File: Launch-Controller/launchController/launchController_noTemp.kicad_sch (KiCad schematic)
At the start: 124 parts, among them J1 Conn_01x05_Pin, J10 Conn_01x05_Pin, J11 Raspberry_Pi_5, J13 26 pin Dsub, J14 DB25_Plug, J15 Conn_01x03_Pin, J16 DB25_Plug, J17 DB25_Plug, J18 Conn_01x03_Pin, J2 Conn_01x05_Pin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

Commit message: polished launch controller layout
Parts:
- J1, J10, J2, J3, J4, J5, J6, J7, J8, J9: footprint launch_controller:Relay Connector -> launch_controller:RelaySwitch Connector
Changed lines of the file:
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@@
 			)
 		)
-		(property "Footprint" "launch_controller:Relay Connector"
+		(property "Footprint" "launch_controller:RelaySwitch Connector"
 			(at 25.4 204.47 0)
 			(effects
@@
 			)
 		)
-		(property "Footprint" "launch_controller:Relay Connector"
+		(property "Footprint" "launch_controller:RelaySwitch Connector"
 			(at 25.4 166.37 0)
 			(effects
@@
 			)
 		)
-		(property "Footprint" "launch_controller:Relay Connector"
+		(property "Footprint" "launch_controller:RelaySwitch Connector"
 			(at 25.4 147.32 0)
 			(effects
@@
 			)
 		)
-		(property "Footprint" "launch_controller:Relay Connector"
+		(property "Footprint" "launch_controller:RelaySwitch Connector"
 			(at 25.4 53.34 0)
 			(effects
@@
 			)
 		)
-		(property "Footprint" "launch_controller:Relay Connector"
+		(property "Footprint" "launch_controller:RelaySwitch Connector"
 			(at 25.4 72.39 0)
 			(effects
@@
 			)
 		)
-		(property "Footprint" "launch_controller:Relay Connector"
+		(property "Footprint" "launch_controller:RelaySwitch Connector"
 			(at 25.4 34.29 0)
 			(effects
@@
 			)
 		)
-		(property "Footprint" "launch_controller:Relay Connector"
+		(property "Footprint" "launch_controller:RelaySwitch Connector"
 			(at 25.4 185.42 0)
 			(effects
@@
 			)
 		)
-		(property "Footprint" "launch_controller:Relay Connector"
+		(property "Footprint" "launch_controller:RelaySwitch Connector"
 			(at 25.4 91.44 0)
 			(effects
@@
 			)
 		)
-		(property "Footprint" "launch_controller:Relay Connector"
+		(property "Footprint" "launch_controller:RelaySwitch Connector"
 			(at 25.4 109.22 0)
 			(effects
@@
 			)
 		)
-		(property "Footprint" "launch_controller:Relay Connector"
+		(property "Footprint" "launch_controller:RelaySwitch Connector"
 			(at 25.4 128.27 0)
 			(effects

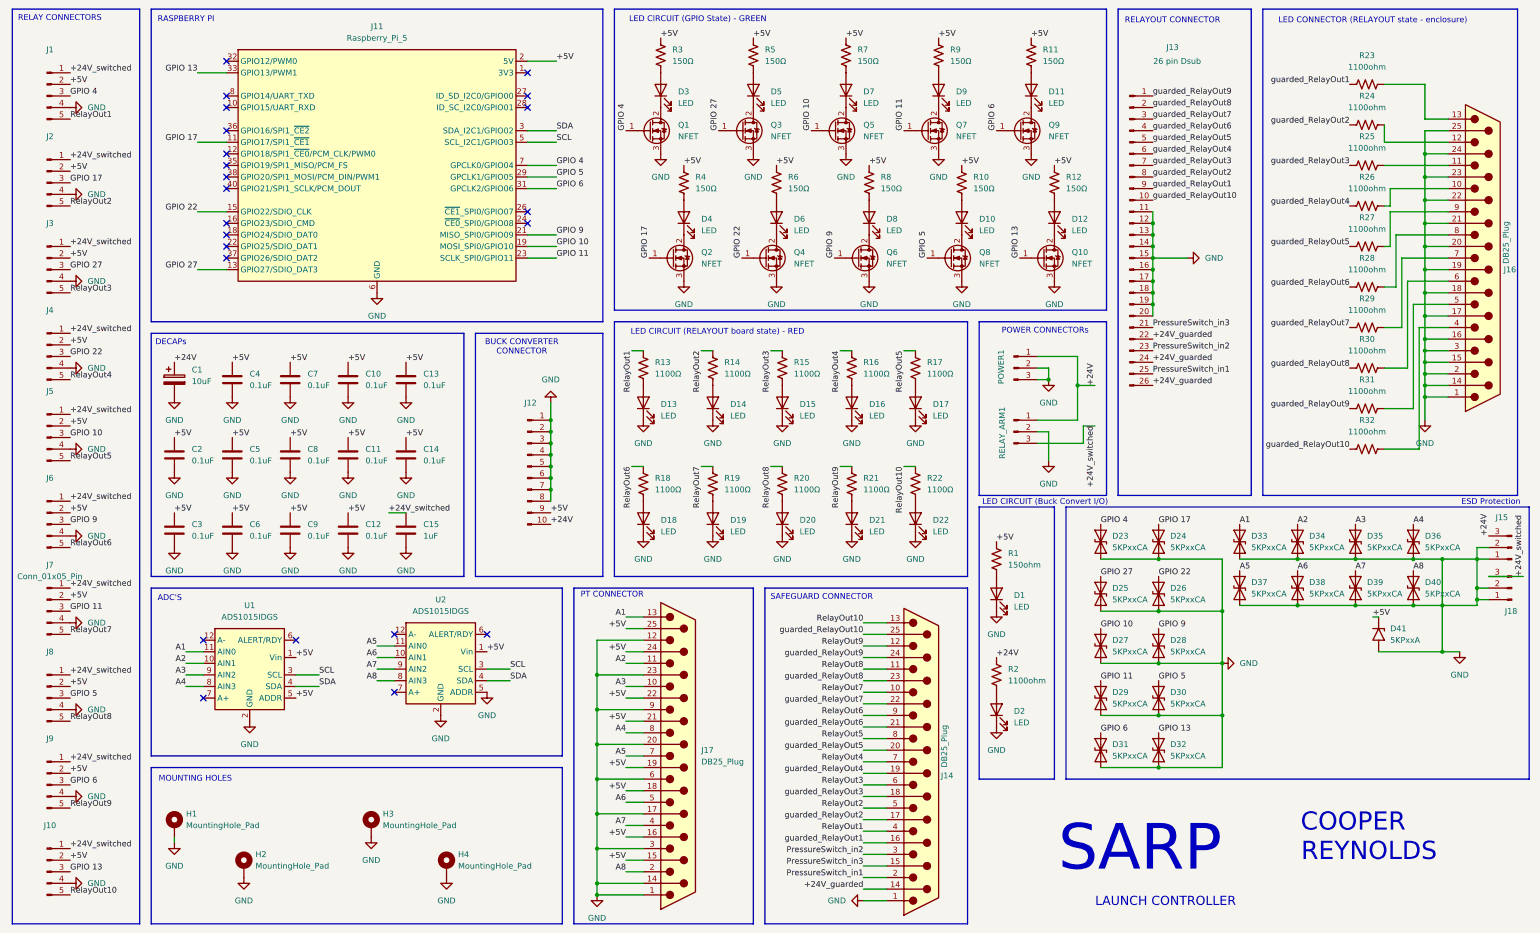
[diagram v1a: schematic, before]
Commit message: logic shifter in LC, cleaning up buck_5v
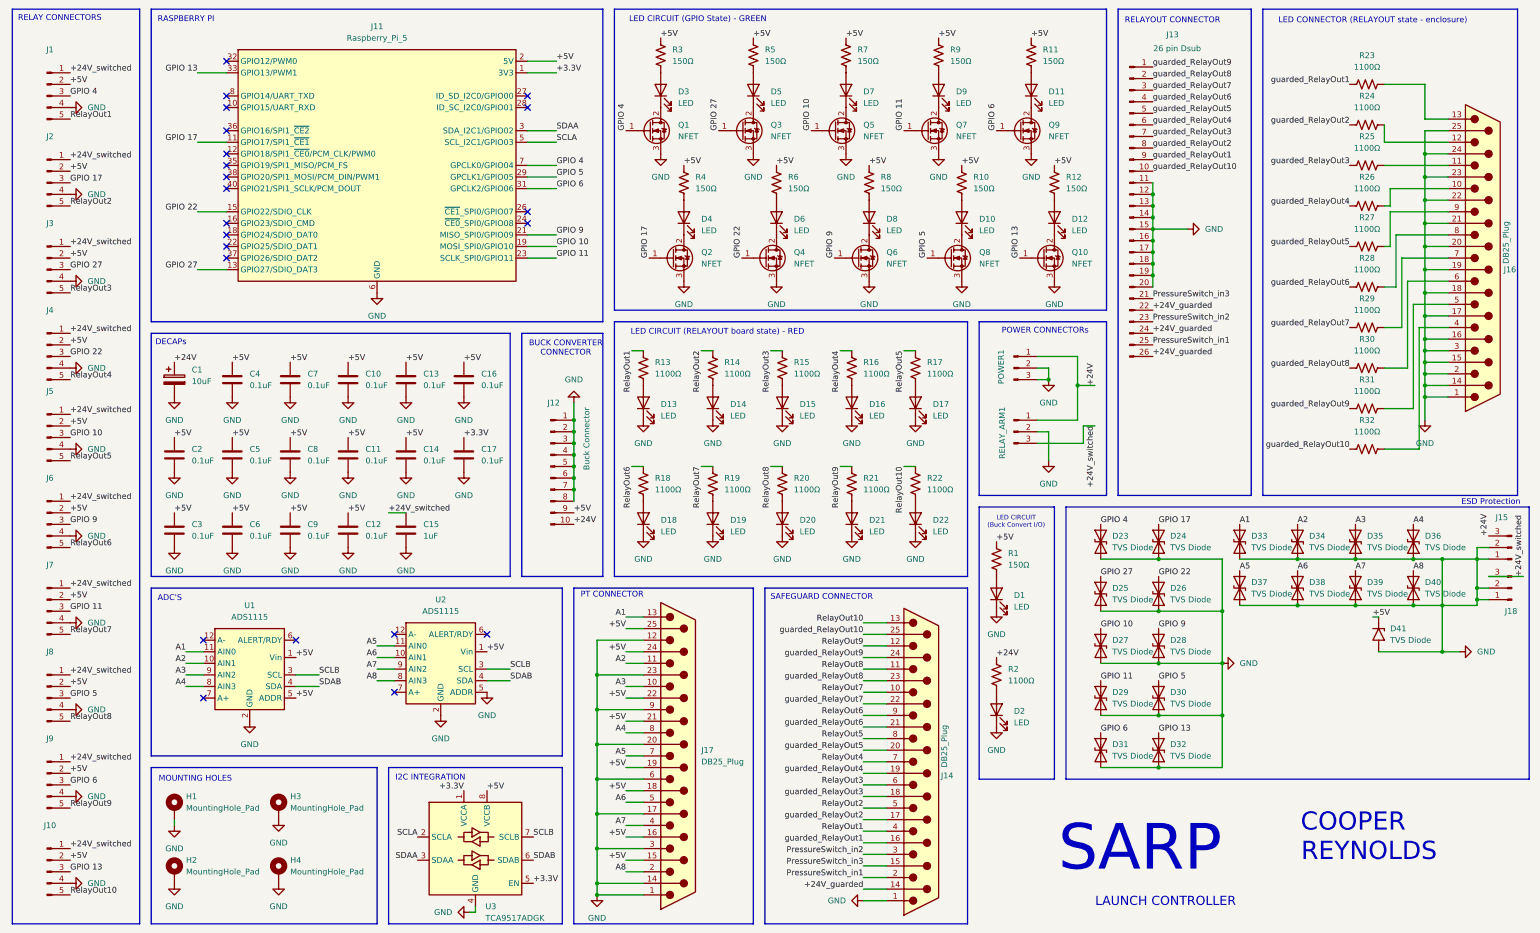
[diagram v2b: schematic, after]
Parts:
- added C16, C17: 0.1uF, Capacitor_SMD:C_0402_1005Metric_Pad0.74x0.62mm_HandSolder, symbol Device:C
- added U3: TCA9517ADGK, Package_SO:Texas_S-PDSO-G8_3x3mm_P0.65mm, symbol Logic_LevelTranslator:TCA9517ADGK
- D23, D24, D25, D26, D27, D28, D29, D30, D31, D32, D33, D34, D35, D36, D37, D38, D39, D40: value 5KPxxCA -> TVS Diode
- D41: value 5KPxxA -> TVS Diode
- J1, J10, J2, J3, J4, J5, J6, J7, J8, J9: value Conn_01x05_Pin -> Relay Connector
- J12: value ~ -> Buck Connector
- J15, J18: value Conn_01x03_Pin -> TVS Diode
- POWER1, RELAY_ARM1: value Conn_01x03_Pin -> Power Connector
- R1: value 150ohm -> 150Ω
- R13, R14, R15, R16, R17, R18, R19, R20, R21, R22: value 1100Ω -> 1100Ω
- R2, R23, R24, R25, R26, R27, R28, R29, R30, R31, R32: value 1100ohm -> 1100Ω
- U1, U2: value ADS1015IDGS -> ADS1115
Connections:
- net +5V: now also C16.1, U3.8 (VCCB)
- net GND: now also C16.2, C17.2, U3.4 (GND)
- net +3.3V: now reaches J11.1 (3V3), J11.17 (3V3)
- net +3.3V: now also C17.1, U3.1 (VCCA), U3.5 (EN)
- net SCL renamed SCLB
- net SCLB: now also U3.7 (SCLB); no longer J11.5 (SCL_I2C1/GPIO03)
- net SDA renamed SDAB
- net SDAB: now also U3.6 (SDAB); no longer J11.3 (SDA_I2C1/GPIO02)
- new net SCLA: J11.5 (SCL_I2C1/GPIO03), U3.2 (SCLA)
- new net SDAA: J11.3 (SDA_I2C1/GPIO02), U3.3 (SDAA)
- no-connect marks 23 -> 22
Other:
- note added: "I2C INTEGRATION"
- moved on the sheet: H1, H2, H3, H4, J12, J13
